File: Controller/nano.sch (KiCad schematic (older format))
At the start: 24 parts, among them J10 ICSP, K1 SW_RESET, U2 INTERFACE-CH340T_SSOP20_, U3 MCU-ATMEGA328P-AU_TQFP32_, Y1 12MHz, Y2 16MHZ

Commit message: More power routing
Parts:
- gave numbers to parts that had none: 1
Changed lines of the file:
@@
 Connection ~ 6800 1400
 $Comp
-L UJ2-BH-1-TH:UJ2-BH-1-TH J?
+L UJ2-BH-1-TH:UJ2-BH-1-TH J15
 U 1 1 5D55598E
 P 3300 2150
-F 0 "J?" H 3407 2617 50  0000 C CNN
+F 0 "J15" H 3407 2617 50  0000 C CNN
 F 1 "UJ2-BH-1-TH" H 3407 2526 50  0000 C CNN
 F 2 "CUI:CUI_UJ2-BH-1-TH" H 3300 2150 50  0001 L BNN

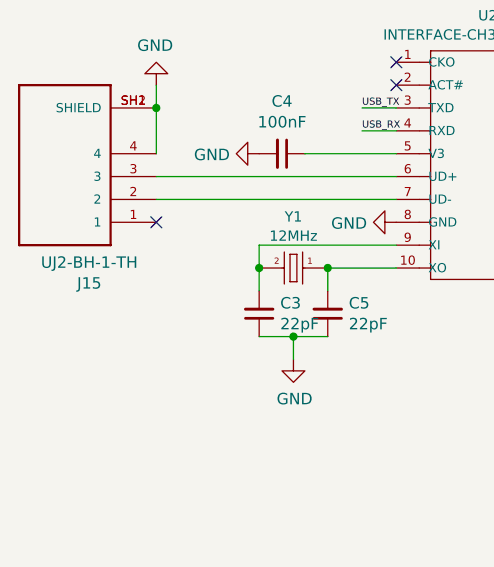
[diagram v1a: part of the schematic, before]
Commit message: Probably giving up on Pi option
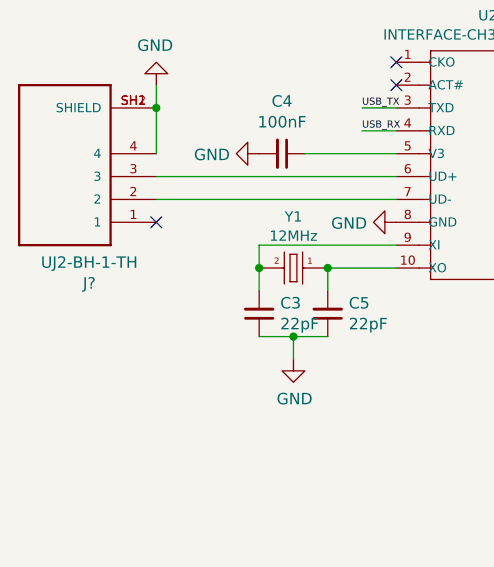
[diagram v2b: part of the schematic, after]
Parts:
- renumbered J15 to J?
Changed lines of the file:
@@
 Connection ~ 6800 1400
 $Comp
-L UJ2-BH-1-TH:UJ2-BH-1-TH J15
+L UJ2-BH-1-TH:UJ2-BH-1-TH J?
 U 1 1 5D55598E
 P 3300 2150
-F 0 "J15" H 3407 2617 50  0000 C CNN
+F 0 "J?" H 3407 2617 50  0000 C CNN
 F 1 "UJ2-BH-1-TH" H 3407 2526 50  0000 C CNN
 F 2 "CUI:CUI_UJ2-BH-1-TH" H 3300 2150 50  0001 L BNN
